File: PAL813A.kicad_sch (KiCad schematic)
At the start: 5 parts, among them U7 74F241_Split, U7 PAL16L8

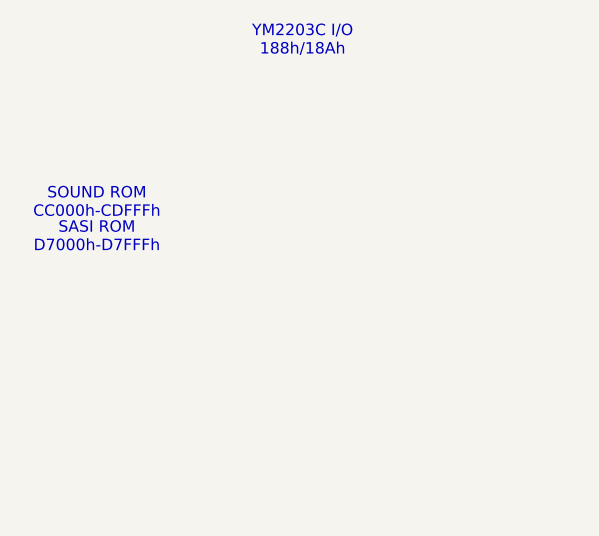
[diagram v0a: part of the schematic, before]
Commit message: Update I/O port table
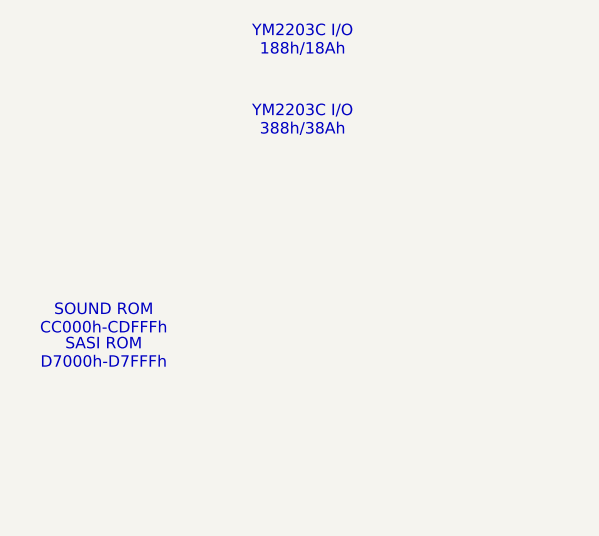
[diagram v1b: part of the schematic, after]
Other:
- note added: "YM2203C I/O 388h/38Ah"
